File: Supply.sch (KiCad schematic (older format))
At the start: 22 parts, among them IC1 B1212S-2W, IC2 JW5052C, IC3 JW5052C

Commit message: - removed rescue lib and symbols - added HSWR.lib
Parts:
- C10, C11, C3, C4: symbol HSWR-V2-rescue:C-Device -> Device:C
- C5, C6, C7, C8: symbol HSWR-V2-rescue:C_Small-Device -> Device:C_Small
- IC1: symbol HSWR-V2-rescue:DCDC_6pin-Auktoralib-HSWR-rescue -> HSWR:DCDC_6pin
- IC2, IC3: symbol HSWR-V2-rescue:JW5052C-Auktoralib-HSWR-rescue -> HSWR:JW5052C
- L1, L2: symbol HSWR-V2-rescue:L-Device -> Device:L
- NT1: symbol HSWR-V2-rescue:Net-Tie_2-Device -> Device:Net-Tie_2
- R12, R13, R14, R15, R16, R17: symbol HSWR-V2-rescue:R_Small-Device -> Device:R_Small
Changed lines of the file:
@@
 $EndDescr
 $Comp
-L HSWR-V2-rescue:Net-Tie_2-Device NT1
+L Device:Net-Tie_2 NT1
 U 1 1 5C9BC448
 P 3850 6600
@@
 $EndComp
 $Comp
-L HSWR-V2-rescue:GND-power #PWR029
+L power:GND #PWR029
 U 1 1 5C9BC4AA
 P 3750 6600
@@
 $EndComp
 $Comp
-L HSWR-V2-rescue:GNDPWR-power #PWR032
+L power:GNDPWR #PWR032
 U 1 1 5C9BC4F1
 P 3950 6600
@@
 $EndComp
 $Comp
-L HSWR-V2-rescue:JW5052C-Auktoralib-HSWR-rescue IC3
+L HSWR:JW5052C IC3
 U 1 1 5C9E348B
 P 3850 5550
@@
 $EndComp
 $Comp
-L HSWR-V2-rescue:C_Small-Device C8
+L Device:C_Small C8
 U 1 1 5C9E3608
 P 4250 5350
@@
 $EndComp
 $Comp
-L HSWR-V2-rescue:L-Device L2
+L Device:L L2
 U 1 1 5C9E3F81
 P 4700 5450
@@
 	4550 5450 4250 5450
 $Comp
-L HSWR-V2-rescue:C-Device C11
+L Device:C C11
 U 1 1 5C9E3FDF
 P 5300 5600
@@
 $EndComp
 $Comp
-L HSWR-V2-rescue:R_Small-Device R16
+L Device:R_Small R16
 U 1 1 5C9E4149
 P 4850 5550
@@
 	1    0    0    -1
 $EndComp
-$Comp
-L HSWR-V2-rescue:R_Small-Device R17
-U 1 1 5C9E4171
-P 4850 5750
-F 0 "R17" H 4909 5796 50  0000 L CNN
-F 1 "11k" H 4909 5705 50  0000 L CNN
-F 2 "Resistor_SMD:R_0805_2012Metric" H 4850 5750 50  0001 C CNN
-F 3 "~" H 4850 5750 50  0001 C CNN
-	1    4850 5750
-	1    0    0    -1
-$EndComp
 Wire Wire Line
 	4850 5450 5300 5450
-Connection ~ 4850 5450
-$Comp
-L HSWR-V2-rescue:GND-power #PWR031
+$Comp
+L power:GND #PWR031
 U 1 1 5C9E41F1
 P 3850 6000
@@
 $EndComp
 $Comp
-L HSWR-V2-rescue:GND-power #PWR036
+L power:GND #PWR036
 U 1 1 5C9E4213
 P 4850 5850
@@
 $EndComp
 $Comp
-L HSWR-V2-rescue:GND-power #PWR040
+L power:GND #PWR040
 U 1 1 5C9E422E
 P 5300 5750
@@
 Wire Wire Line
 	4250 5650 4850 5650
-Connection ~ 4850 5650
-$Comp
-L HSWR-V2-rescue:R_Small-Device R13
+$Comp
+L Device:R_Small R13
 U 1 1 5C9E4723
 P 3450 5350
@@
 $EndComp
 $Comp
-L HSWR-V2-rescue:C-Device C4
+L Device:C C4
 U 1 1 5C9E4C14
 P 3150 5600
@@
 $EndComp
 $Comp
-L HSWR-V2-rescue:GND-power #PWR026
+L power:GND #PWR026
 U 1 1 5C9E4C52
 P 3150 5750
@@
 	3150 5250 3450 5250
 $Comp
-L HSWR-V2-rescue:+3V3-power #PWR039
+L power:+3V3 #PWR039
 U 1 1 5C9E5148
 P 5300 5450
@@
 	1    0    0    -1
 $EndComp
-Connection ~ 5300 5450
-$Comp
-L HSWR-V2-rescue:JW5052C-Auktoralib-HSWR-rescue IC2
+$Comp
+L HSWR:JW5052C IC2
 U 1 1 5C9E68F7
 P 3850 4150
@@
 $EndComp
 $Comp
-L HSWR-V2-rescue:C_Small-Device C7
+L Device:C_Small C7
 U 1 1 5C9E68FD
 P 4250 3950
@@
 $EndComp
 $Comp
-L HSWR-V2-rescue:L-Device L1
+L Device:L L1
 U 1 1 5C9E6903
 P 4700 4050
@@
 	4550 4050 4250 4050
 $Comp
-L HSWR-V2-rescue:C-Device C10
+L Device:C C10
 U 1 1 5C9E690B
 P 5300 4200
@@
 $EndComp
 $Comp
-L HSWR-V2-rescue:R_Small-Device R14
+L Device:R_Small R14
 U 1 1 5C9E6911
 P 4850 4150
@@
 $EndComp
 $Comp
-L HSWR-V2-rescue:R_Small-Device R15
+L Device:R_Small R15
 U 1 1 5C9E6917
 P 4850 4350
@@
 Wire Wire Line
 	4850 4050 5300 4050
-Connection ~ 4850 4050
-$Comp
-L HSWR-V2-rescue:GND-power #PWR030
+$Comp
+L power:GND #PWR030
 U 1 1 5C9E691F
 P 3850 4600
@@
 $EndComp
 $Comp
-L HSWR-V2-rescue:GND-power #PWR035
+L power:GND #PWR035
 U 1 1 5C9E6925
 P 4850 4450
@@
 $EndComp
 $Comp
-L HSWR-V2-rescue:GND-power #PWR038
+L power:GND #PWR038
 U 1 1 5C9E692B
 P 5300 4350
@@
 Wire Wire Line
 	4250 4250 4850 4250
-Connection ~ 4850 4250
-$Comp
-L HSWR-V2-rescue:R_Small-Device R12
+$Comp
+L Device:R_Small R12
 U 1 1 5C9E6933
 P 3450 3950
@@
 $EndComp
 $Comp
-L HSWR-V2-rescue:C-Device C3
+L Device:C C3
 U 1 1 5C9E6939
 P 3150 4200
@@
 $EndComp
 $Comp
-L HSWR-V2-rescue:GND-power #PWR024
+L power:GND #PWR024
 U 1 1 5C9E693F
 P 3150 4350
@@
 	3150 3850 3450 3850
 $Comp
-L HSWR-V2-rescue:+12V-power #PWR023
+L power:+12V #PWR023
 U 1 1 5C9E6948
 P 3150 3850
@@
 	1    0    0    -1
 $EndComp
-Connection ~ 3150 3850
-$Comp
-L HSWR-V2-rescue:+5V-power #PWR037
+$Comp
+L power:+5V #PWR037
 U 1 1 5C9E6DAC
 P 5300 4050
@@
 	1    0    0    -1
 $EndComp
-Connection ~ 5300 4050
-$Comp
-L HSWR-V2-rescue:+5V-power #PWR025
+$Comp
+L power:+5V #PWR025
 U 1 1 5C9E7E71
 P 3150 5250
@@
 	1    0    0    -1
 $EndComp
-Connection ~ 3150 5250
-$Comp
-L HSWR-V2-rescue:C_Small-Device C5
+$Comp
+L Device:C_Small C5
 U 1 1 5C9EB58E
 P 3450 2900
@@
 $EndComp
 $Comp
-L HSWR-V2-rescue:C_Small-Device C6
+L Device:C_Small C6
 U 1 1 5C9EB75E
 P 4250 2800
@@
 $EndComp
 $Comp
-L HSWR-V2-rescue:Earth-power #PWR028
-U 1 1 5C9EBAE0
-P 3450 3000
-F 0 "#PWR028" H 3450 2750 50  0001 C CNN
-F 1 "Earth" H 3450 2850 50  0001 C CNN
-F 2 "" H 3450 3000 50  0001 C CNN
-F 3 "~" H 3450 3000 50  0001 C CNN
-	1    3450 3000
-	1    0    0    -1
-$EndComp
-$Comp
-L HSWR-V2-rescue:GND-power #PWR034
+L power:GND #PWR034
 U 1 1 5C9EBC32
 P 4250 3100
@@
 $EndComp
 $Comp
-L HSWR-V2-rescue:+12VA-power #PWR027
+L power:+12VA #PWR027
 U 1 1 5C9F009D
 P 3450 2800
@@
 $EndComp
 $Comp
-L HSWR-V2-rescue:+12V-power #PWR033
+L power:+12V #PWR033
 U 1 1 5C9F02AD
 P 4250 2700
@@
 $EndComp
 $Comp
-L HSWR-V2-rescue:DCDC_6pin-Auktoralib-HSWR-rescue IC1
+L HSWR:DCDC_6pin IC1
 U 1 1 5C9F1AAA
 P 3850 2900
@@
 Wire Wire Line
 	4250 2900 4250 3100
-Connection ~ 4250 2900
-Connection ~ 4250 3100
 $Comp
 L Device:CP_Small C9
@@
 Wire Wire Line
 	4600 2700 4250 2700
-Connection ~ 4250 2700
 Wire Wire Line
 	4600 2900 4250 2900
@@
 Wire Wire Line
 	3450 2800 3100 2800
+Wire Wire Line
+	3450 3000 3100 3000
+Connection ~ 4250 2900
+Connection ~ 4250 2700
 Connection ~ 3450 2800
-Wire Wire Line
-	3450 3000 3100 3000
 Connection ~ 3450 3000
+$Comp
+L power:Earth #PWR028
+U 1 1 5C9EBAE0
+P 3450 3000
+F 0 "#PWR028" H 3450 2750 50  0001 C CNN
+F 1 "Earth" H 3450 2850 50  0001 C CNN
+F 2 "" H 3450 3000 50  0001 C CNN
+F 3 "~" H 3450 3000 50  0001 C CNN
+	1    3450 3000
+	1    0    0    -1
+$EndComp
+$Comp
+L Device:R_Small R17
+U 1 1 5C9E4171
+P 4850 5750
+F 0 "R17" H 4909 5796 50  0000 L CNN
+F 1 "11k" H 4909 5705 50  0000 L CNN
+F 2 "Resistor_SMD:R_0805_2012Metric" H 4850 5750 50  0001 C CNN
+F 3 "~" H 4850 5750 50  0001 C CNN
+	1    4850 5750
+	1    0    0    -1
+$EndComp
+Connection ~ 4850 5650
+Connection ~ 4850 5450
+Connection ~ 4250 5450
+Connection ~ 3450 5250
+Connection ~ 3150 5250
+Connection ~ 5300 5450
+Connection ~ 5300 4050
+Connection ~ 4850 4050
+Connection ~ 4850 4250
+Connection ~ 4250 4050
 Connection ~ 3450 3850
-Connection ~ 4250 4050
-Connection ~ 3450 5250
-Connection ~ 4250 5450
+Connection ~ 3150 3850
 $EndSCHEMATC

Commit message: - updated schematic symbols - updated silk screen version label
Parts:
- C2, C9: symbol Device:CP_Small -> Device:C_Polarized_Small
- NT1: symbol Device:Net-Tie_2 -> Device:NetTie_2
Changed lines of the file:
@@
 $EndDescr
 $Comp
-L Device:Net-Tie_2 NT1
+L Device:NetTie_2 NT1
 U 1 1 5C9BC448
 P 3850 6600
@@
 	4250 2900 4250 3100
 $Comp
-L Device:CP_Small C9
+L Device:C_Polarized_Small C9
 U 1 1 5E227FE9
 P 4600 2800
@@
 	4600 2900 4250 2900
 $Comp
-L Device:CP_Small C2
+L Device:C_Polarized_Small C2
 U 1 1 5E22948F
 P 3100 2900

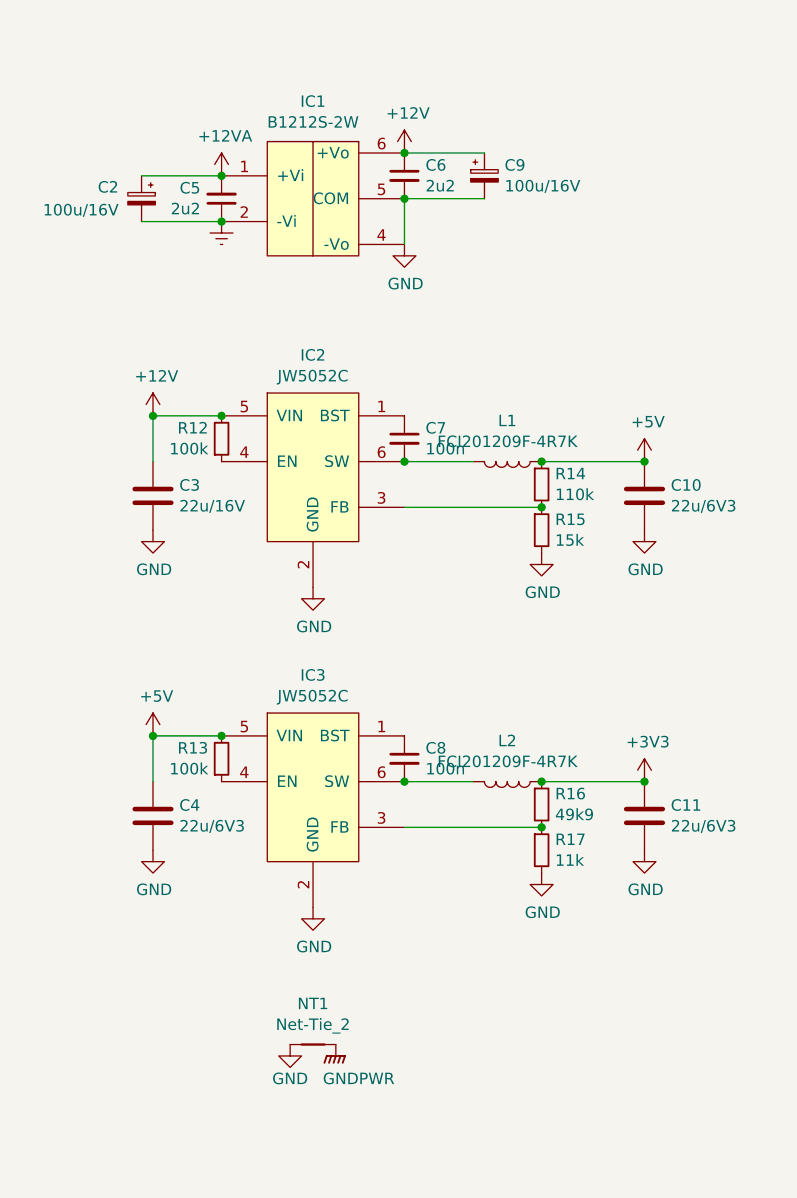
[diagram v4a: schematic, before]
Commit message: - removed 5V DCDC because unused
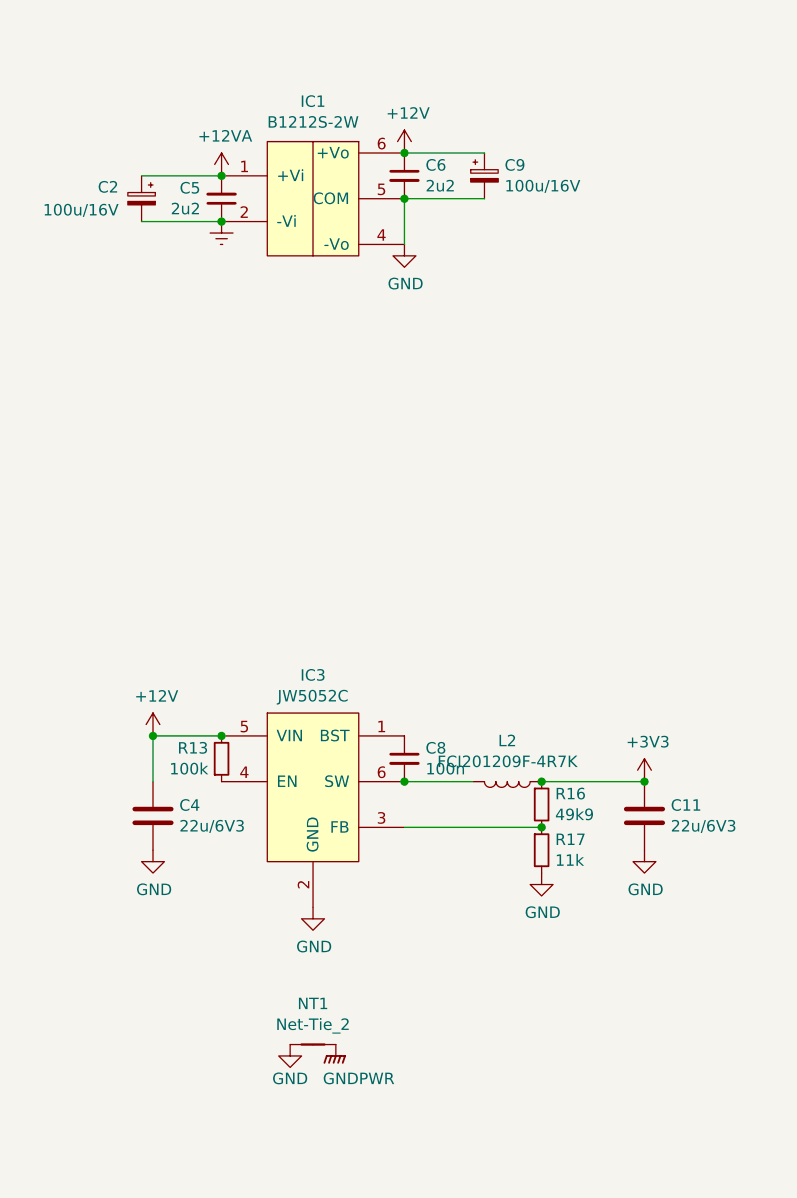
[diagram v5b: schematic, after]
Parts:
- removed C10: 22u/6V3, Capacitor_SMD:C_0805_2012Metric, symbol Device:C
- removed C3: 22u/16V, Capacitor_SMD:C_0805_2012Metric, symbol Device:C
- removed C7: 100n, Capacitor_SMD:C_0805_2012Metric, symbol Device:C_Small
- removed IC2: JW5052C, Package_TO_SOT_SMD:TSOT-23-6, symbol HSWR:JW5052C
- removed L1: FCI201209F-4R7K, Inductor_SMD:L_0805_2012Metric, symbol Device:L
- removed R12: 100k, Resistor_SMD:R_0805_2012Metric, symbol Device:R_Small
- removed R14: 110k, Resistor_SMD:R_0805_2012Metric, symbol Device:R_Small
- removed R15: 15k, Resistor_SMD:R_0805_2012Metric, symbol Device:R_Small
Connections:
- net +5V is gone; now on net +12V: C4.1, IC3.5 (VIN), R13.2
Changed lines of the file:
@@
 $EndComp
-$Comp
-L HSWR:JW5052C IC2
-U 1 1 5C9E68F7
-P 3850 4150
-F 0 "IC2" H 3850 4715 50  0000 C CNN
-F 1 "JW5052C" H 3850 4624 50  0000 C CNN
-F 2 "Package_TO_SOT_SMD:TSOT-23-6" H 5700 5150 50  0001 C CNN
-F 3 "" H 5700 5150 50  0001 C CNN
-	1    3850 4150
-	1    0    0    -1
-$EndComp
-$Comp
-L Device:C_Small C7
-U 1 1 5C9E68FD
-P 4250 3950
-F 0 "C7" H 4342 3996 50  0000 L CNN
-F 1 "100n" H 4342 3905 50  0000 L CNN
-F 2 "Capacitor_SMD:C_0805_2012Metric" H 4250 3950 50  0001 C CNN
-F 3 "~" H 4250 3950 50  0001 C CNN
-	1    4250 3950
-	1    0    0    -1
-$EndComp
-$Comp
-L Device:L L1
-U 1 1 5C9E6903
-P 4700 4050
-F 0 "L1" V 4522 4050 50  0000 C CNN
-F 1 "FCI201209F-4R7K" V 4613 4050 50  0000 C CNN
-F 2 "Inductor_SMD:L_0805_2012Metric" H 4700 4050 50  0001 C CNN
-F 3 "~" H 4700 4050 50  0001 C CNN
-	1    4700 4050
-	0    1    1    0
-$EndComp
-Wire Wire Line
-	4550 4050 4250 4050
-$Comp
-L Device:C C10
-U 1 1 5C9E690B
-P 5300 4200
-F 0 "C10" H 5415 4246 50  0000 L CNN
-F 1 "22u/6V3" H 5415 4155 50  0000 L CNN
-F 2 "Capacitor_SMD:C_0805_2012Metric" H 5338 4050 50  0001 C CNN
-F 3 "~" H 5300 4200 50  0001 C CNN
-	1    5300 4200
-	1    0    0    -1
-$EndComp
-$Comp
-L Device:R_Small R14
-U 1 1 5C9E6911
-P 4850 4150
-F 0 "R14" H 4909 4196 50  0000 L CNN
-F 1 "110k" H 4909 4105 50  0000 L CNN
-F 2 "Resistor_SMD:R_0805_2012Metric" H 4850 4150 50  0001 C CNN
-F 3 "~" H 4850 4150 50  0001 C CNN
-	1    4850 4150
-	1    0    0    -1
-$EndComp
-$Comp
-L Device:R_Small R15
-U 1 1 5C9E6917
-P 4850 4350
-F 0 "R15" H 4909 4396 50  0000 L CNN
-F 1 "15k" H 4909 4305 50  0000 L CNN
-F 2 "Resistor_SMD:R_0805_2012Metric" H 4850 4350 50  0001 C CNN
-F 3 "~" H 4850 4350 50  0001 C CNN
-	1    4850 4350
-	1    0    0    -1
-$EndComp
-Wire Wire Line
-	4850 4050 5300 4050
-$Comp
-L power:GND #PWR030
-U 1 1 5C9E691F
-P 3850 4600
-F 0 "#PWR030" H 3850 4350 50  0001 C CNN
-F 1 "GND" H 3855 4427 50  0000 C CNN
-F 2 "" H 3850 4600 50  0001 C CNN
-F 3 "" H 3850 4600 50  0001 C CNN
-	1    3850 4600
-	1    0    0    -1
-$EndComp
-$Comp
-L power:GND #PWR035
-U 1 1 5C9E6925
-P 4850 4450
-F 0 "#PWR035" H 4850 4200 50  0001 C CNN
-F 1 "GND" H 4855 4277 50  0000 C CNN
-F 2 "" H 4850 4450 50  0001 C CNN
-F 3 "" H 4850 4450 50  0001 C CNN
-	1    4850 4450
-	1    0    0    -1
-$EndComp
-$Comp
-L power:GND #PWR038
-U 1 1 5C9E692B
-P 5300 4350
-F 0 "#PWR038" H 5300 4100 50  0001 C CNN
-F 1 "GND" H 5305 4177 50  0000 C CNN
-F 2 "" H 5300 4350 50  0001 C CNN
-F 3 "" H 5300 4350 50  0001 C CNN
-	1    5300 4350
-	1    0    0    -1
-$EndComp
-Wire Wire Line
-	4250 4250 4850 4250
-$Comp
-L Device:R_Small R12
-U 1 1 5C9E6933
-P 3450 3950
-F 0 "R12" H 3392 3904 50  0000 R CNN
-F 1 "100k" H 3392 3995 50  0000 R CNN
-F 2 "Resistor_SMD:R_0805_2012Metric" H 3450 3950 50  0001 C CNN
-F 3 "~" H 3450 3950 50  0001 C CNN
-	1    3450 3950
-	1    0    0    1
-$EndComp
-$Comp
-L Device:C C3
-U 1 1 5C9E6939
-P 3150 4200
-F 0 "C3" H 3265 4246 50  0000 L CNN
-F 1 "22u/16V" H 3265 4155 50  0000 L CNN
-F 2 "Capacitor_SMD:C_0805_2012Metric" H 3188 4050 50  0001 C CNN
-F 3 "~" H 3150 4200 50  0001 C CNN
-	1    3150 4200
-	1    0    0    -1
-$EndComp
-$Comp
-L power:GND #PWR024
-U 1 1 5C9E693F
-P 3150 4350
-F 0 "#PWR024" H 3150 4100 50  0001 C CNN
-F 1 "GND" H 3155 4177 50  0000 C CNN
-F 2 "" H 3150 4350 50  0001 C CNN
-F 3 "" H 3150 4350 50  0001 C CNN
-	1    3150 4350
-	1    0    0    -1
-$EndComp
-Wire Wire Line
-	3150 4050 3150 3850
-Wire Wire Line
-	3150 3850 3450 3850
 $Comp
 L power:+12V #PWR023
 U 1 1 5C9E6948
-P 3150 3850
-F 0 "#PWR023" H 3150 3700 50  0001 C CNN
-F 1 "+12V" H 3165 4023 50  0000 C CNN
-F 2 "" H 3150 3850 50  0001 C CNN
-F 3 "" H 3150 3850 50  0001 C CNN
-	1    3150 3850
-	1    0    0    -1
-$EndComp
-$Comp
-L power:+5V #PWR037
-U 1 1 5C9E6DAC
-P 5300 4050
-F 0 "#PWR037" H 5300 3900 50  0001 C CNN
-F 1 "+5V" H 5315 4223 50  0000 C CNN
-F 2 "" H 5300 4050 50  0001 C CNN
-F 3 "" H 5300 4050 50  0001 C CNN
-	1    5300 4050
-	1    0    0    -1
-$EndComp
-$Comp
-L power:+5V #PWR025
-U 1 1 5C9E7E71
 P 3150 5250
-F 0 "#PWR025" H 3150 5100 50  0001 C CNN
-F 1 "+5V" H 3165 5423 50  0000 C CNN
+F 0 "#PWR023" H 3150 5100 50  0001 C CNN
+F 1 "+12V" H 3165 5423 50  0000 C CNN
 F 2 "" H 3150 5250 50  0001 C CNN
 F 3 "" H 3150 5250 50  0001 C CNN
@@
 Connection ~ 4250 5450
 Connection ~ 3450 5250
+Connection ~ 5300 5450
 Connection ~ 3150 5250
-Connection ~ 5300 5450
-Connection ~ 5300 4050
-Connection ~ 4850 4050
-Connection ~ 4850 4250
-Connection ~ 4250 4050
-Connection ~ 3450 3850
-Connection ~ 3150 3850
 $EndSCHEMATC
